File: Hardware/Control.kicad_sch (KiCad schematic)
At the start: 37 parts, among them J1 XKTF-015-N, SW1 PTS_647_SN50_SMTR2_LFS, SW2 PTS_647_SN50_SMTR2_LFS, SW3 PTS_647_SN50_SMTR2_LFS, U1 RP2354B, X2 ABM8-272-T3

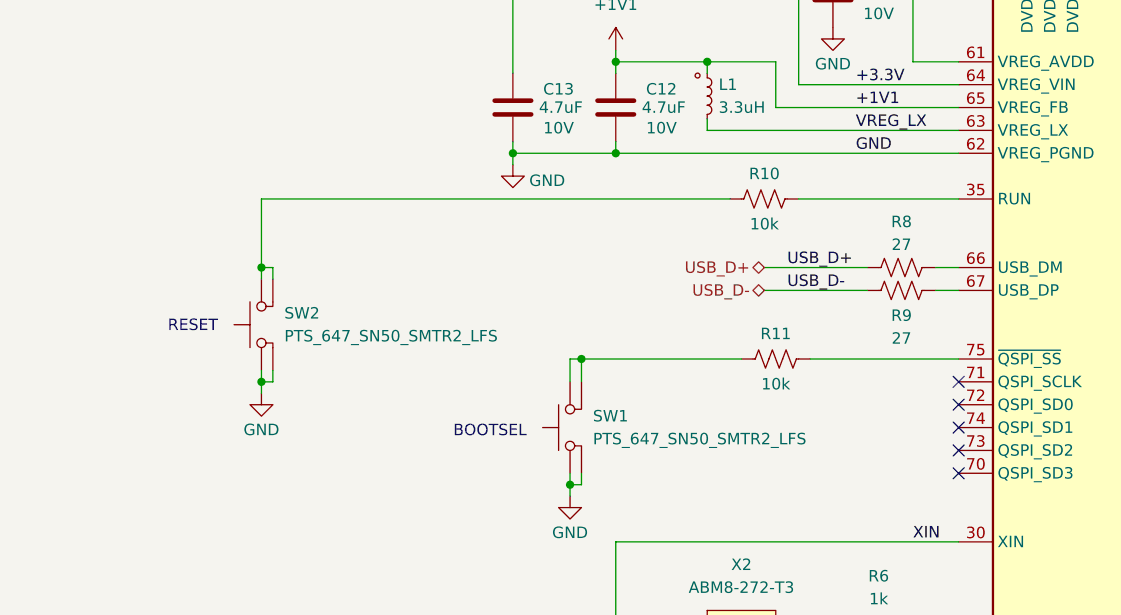
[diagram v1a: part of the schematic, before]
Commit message: fix reset and bootsel pulldowns
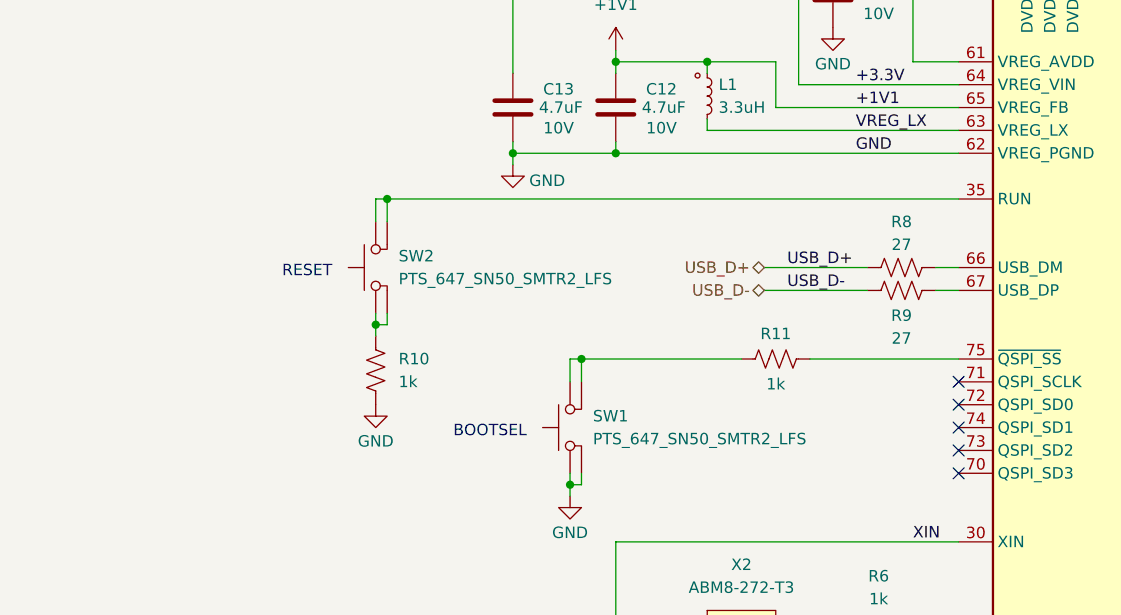
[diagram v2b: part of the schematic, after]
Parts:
- R10, R11: value 10k -> 1k
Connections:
- net GND: now also R10.1; no longer SW2.1, SW2.2
- net at U1.35 (RUN): now also SW2.3, SW2.4; no longer R10.1
- new net: R10.2, SW2.1, SW2.2
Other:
- moved on the sheet: SW2

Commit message: decouple SD card
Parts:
- added C48: 10uF, symbol Device:C
- added R28, R29, R30, R31: 10k, symbol Device:R_US
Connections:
- net +3.3V: now also C48.1, R28.2, R29.2, R30.2, R31.2
- net GND: now also C48.2
- net SD_MISO: now also R31.1
- net SD_MOSI: now also R29.1
- net SD_SCK: now also R30.1
- net ~{SD_CS}: now also R28.1
